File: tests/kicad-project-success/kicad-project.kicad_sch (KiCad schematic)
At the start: 3 parts, among them SW101 SW_Push

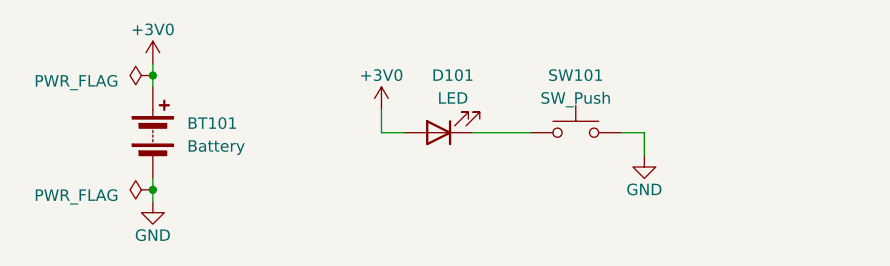
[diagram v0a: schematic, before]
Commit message: Added symbol library support
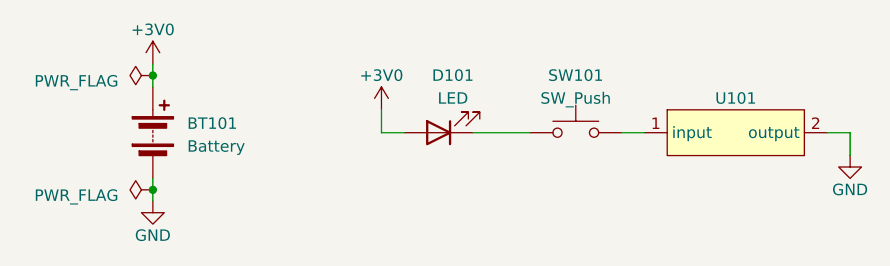
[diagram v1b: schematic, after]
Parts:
- added U101: ~, Capacitor_SMD:CP_Elec_3x5.3, symbol test-library:Line
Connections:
- net GND: now also U101.2 (output); no longer SW101.2
- new net: SW101.2, U101.1 (input)
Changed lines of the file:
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@@
 	(wire
 		(pts
-			(xy 167.64 97.79) (xy 170.18 97.79)
+			(xy 190.5 97.79) (xy 193.04 97.79)
 		)
 		(stroke
@@
 	(wire
 		(pts
+			(xy 170.18 97.79) (xy 167.64 97.79)
+		)
+		(stroke
+			(width 0)
+			(type default)
+		)
+	)
+	(wire
+		(pts
 			(xy 151.13 97.79) (xy 157.48 97.79)
 		)
@@
 	(wire
 		(pts
-			(xy 170.18 97.79) (xy 170.18 100.33)
+			(xy 193.04 97.79) (xy 193.04 100.33)
 		)
 		(stroke
@@
 	)
 	(symbol
+		(lib_id "test-library:Line")
+		(at 180.34 97.79 0)
+		(unit 1)
+		(exclude_from_sim no)
+		(in_bom yes)
+		(on_board yes)
+		(dnp no)
+		(property "Reference" "U101"
+			(at 180.34 93.98 0)
+			(effects
+				(font
+					(size 1.27 1.27)
+				)
+			)
+		)
+		(property "Value" "~"
+			(at 180.34 93.98 0)
+			(effects
+				(font
+					(size 1.27 1.27)
+				)
+			)
+		)
+		(property "Footprint" "Capacitor_SMD:CP_Elec_3x5.3"
+			(at 180.34 97.79 0)
+			(effects
+				(font
+					(size 1.27 1.27)
+				)
+				(hide yes)
+			)
+		)
+		(property "Datasheet" ""
+			(at 180.34 97.79 0)
+			(effects
+				(font
+					(size 1.27 1.27)
+				)
+				(hide yes)
+			)
+		)
+		(property "Description" ""
+			(at 180.34 97.79 0)
+			(effects
+				(font
+					(size 1.27 1.27)
+				)
+				(hide yes)
+			)
+		)
+		(pin "1"
+		)
+		(pin "2"
+		)
+		(instances
+			(project ""
+				(path "/1f7c97ad-5ffd-41dc-a255-91ef2d48b9f7"
+					(reference "U101")
+					(unit 1)
+				)
+			)
+		)
+	)
+	(symbol
 		(lib_id "power:PWR_FLAG")
 		(at 115.57 104.14 90)
@@
 	(symbol
 		(lib_id "power:GND")
-		(at 170.18 100.33 0)
+		(at 193.04 100.33 0)
 		(unit 1)
 		(exclude_from_sim no)
@@
 		(dnp no)
 		(property "Reference" "#PWR0101"
-			(at 170.18 106.68 0)
+			(at 193.04 106.68 0)
 			(effects
 				(font
@@
 		)
 		(property "Value" "GND"
-			(at 170.18 104.14 0)
+			(at 193.04 104.14 0)
 			(effects
 				(font
@@
 		)
 		(property "Footprint" ""
-			(at 170.18 100.33 0)
+			(at 193.04 100.33 0)
 			(effects
 				(font
@@
 		)
 		(property "Datasheet" ""
-			(at 170.18 100.33 0)
+			(at 193.04 100.33 0)
 			(effects
 				(font
@@
 		)
 		(property "Description" "Power symbol creates a global label with name \"GND\" , ground"
-			(at 170.18 100.33 0)
-			(effects
-				(font
+			(at 193.04 100.33 0)
+			(effects
+				(font

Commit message: Fixed error in symbol library
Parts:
- U101: symbol test-library:Line -> test-sym-library:Line
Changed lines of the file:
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@@
 	)
 	(symbol
-		(lib_id "test-library:Line")
+		(lib_id "test-sym-library:Line")
 		(at 180.34 97.79 0)
 		(unit 1)

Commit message: Added footprint library support
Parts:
- U101: footprint Capacitor_SMD:CP_Elec_3x5.3 -> test-fp-library:Line
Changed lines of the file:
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@@
 			)
 		)
-		(property "Footprint" "Capacitor_SMD:CP_Elec_3x5.3"
+		(property "Footprint" "test-fp-library:Line"
 			(at 180.34 97.79 0)
 			(effects
